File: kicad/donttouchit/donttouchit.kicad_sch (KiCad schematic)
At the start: 52 parts, among them J1 Conn_01x02_Female, J10 Conn_01x04_Male, J2 Conn_01x02_Female, J3 Conn_01x02_Female, J4 Conn_01x02_Female, J5 Conn_01x02_Female, J6 Conn_01x02_Female, J7 Conn_01x02_Female, J8 Conn_01x02_Female, J9 Conn_01x02_Female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

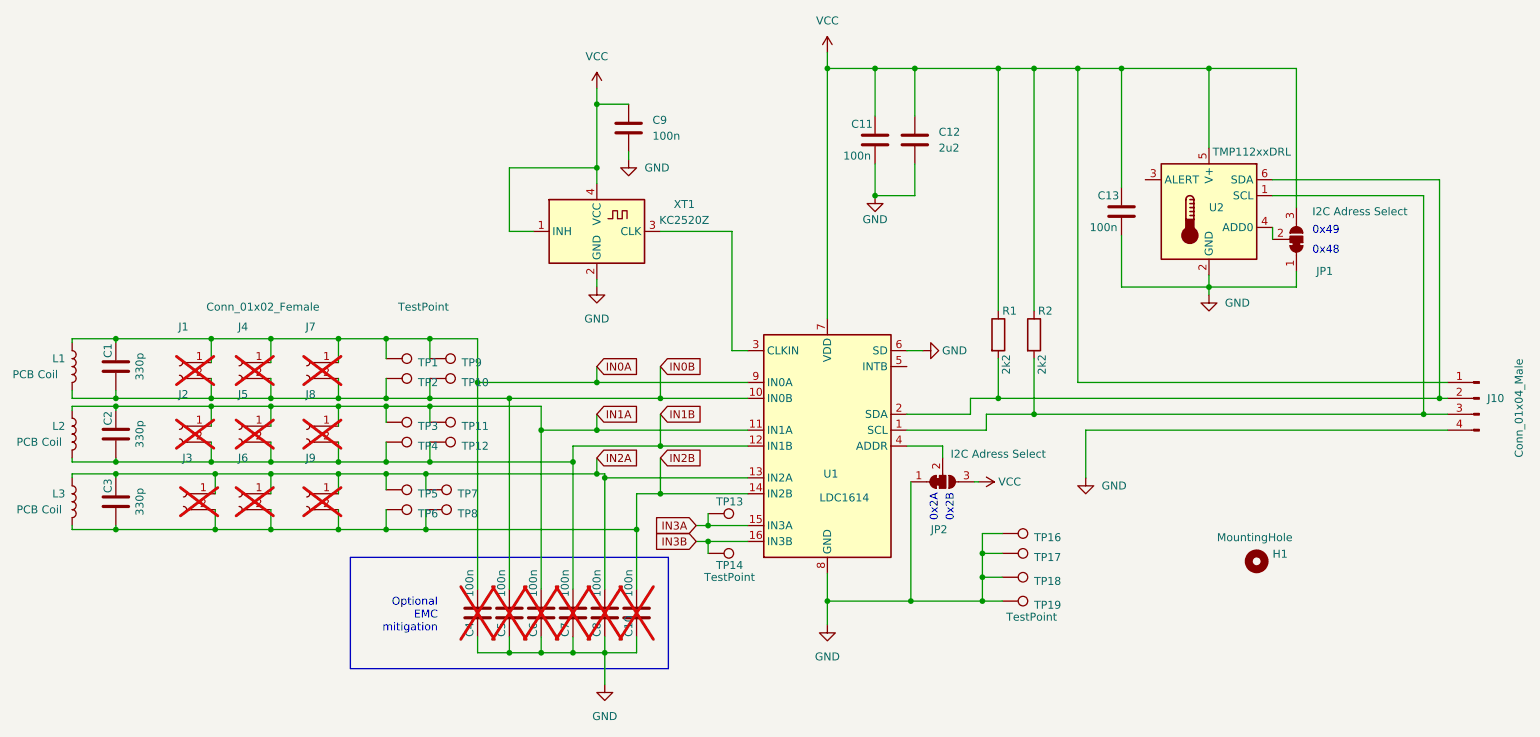
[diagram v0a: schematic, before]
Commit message: smaller formfactor that fits in the space of an Omron probe, 4th sensor pads removed
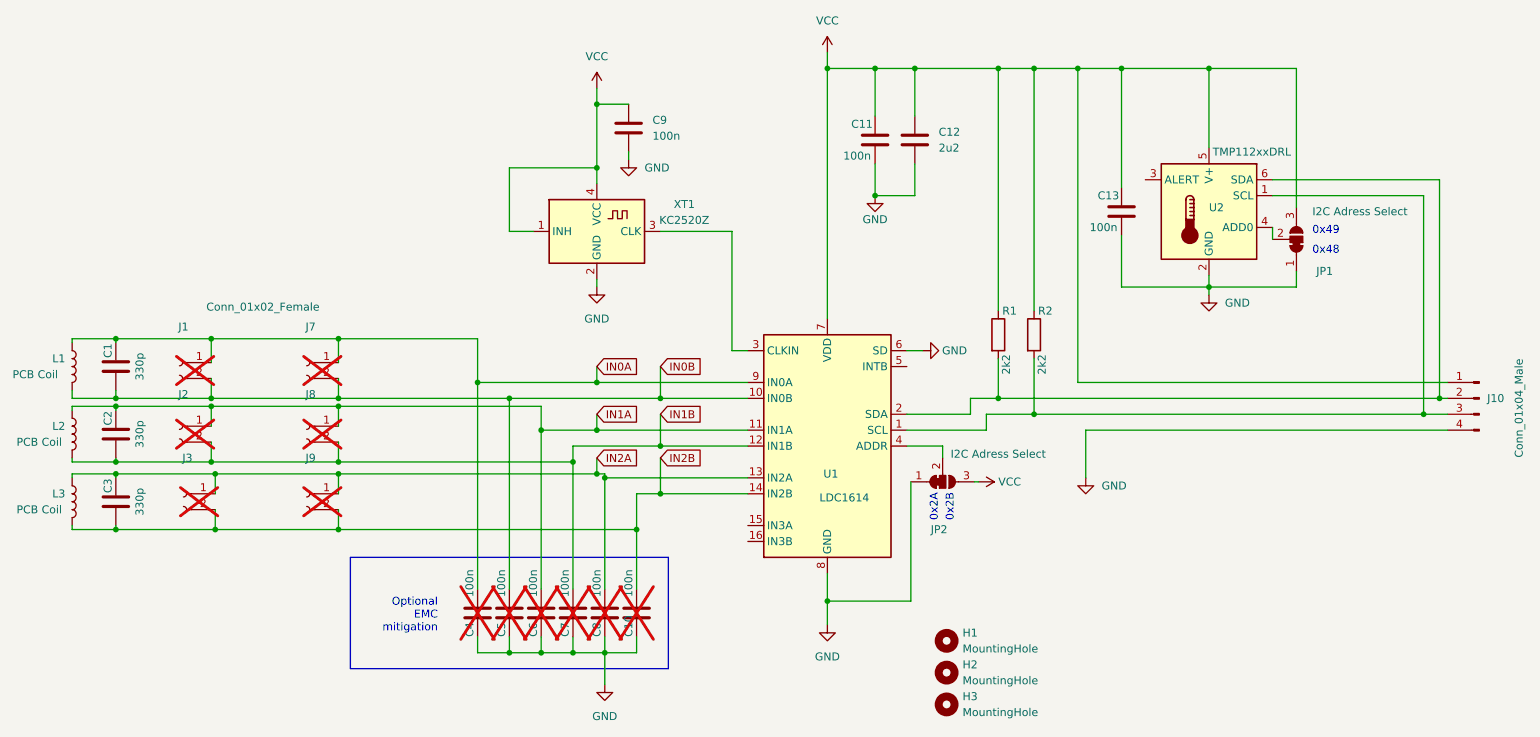
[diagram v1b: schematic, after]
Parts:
- removed J4, J5, J6: Conn_01x02_Female, Library:PCBConnPads, symbol Connector:Conn_01x02_Female
- removed TP1, TP10, TP11, TP12, TP13, TP14, TP16, TP17, TP18, TP19, TP2, TP3, TP4, TP5, TP6, TP7, TP8, TP9: TestPoint, TestPoint:TestPoint_THTPad_1.5x1.5mm_Drill0.7mm, symbol Connector:TestPoint
- added H2, H3: MountingHole, MountingHole:MountingHole_3.5mm, symbol Mechanical:MountingHole
- H1: footprint MountingHole:MountingHole_3.2mm_M3 -> MountingHole:MountingHole_3.5mm
- J1, J2, J3: footprint Library:PCBConnPads -> Library:PCBConnPadsTHT
- J7, J8, J9: footprint Library:PCBConnPadsLong -> Library:PCBConnPadsTHT
- L1, L2, L3: footprint Library:Coil -> Library:Coil_14x14
- U1: footprint Package_DFN_QFN:WQFN-16-1EP_4x4mm_P0.5mm_EP2.6x2.6mm_ThermalVias -> Library:WQFN-16-1EP_4x4mm_P0.5mm_EP2.6x2.6mm_ThermalVias
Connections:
- net IN3A: no longer names the net of U1.15 (IN3A)
- net IN3B: no longer names the net of U1.16 (IN3B)

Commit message: ESD capacitor values corrected / Tempsensor name updated
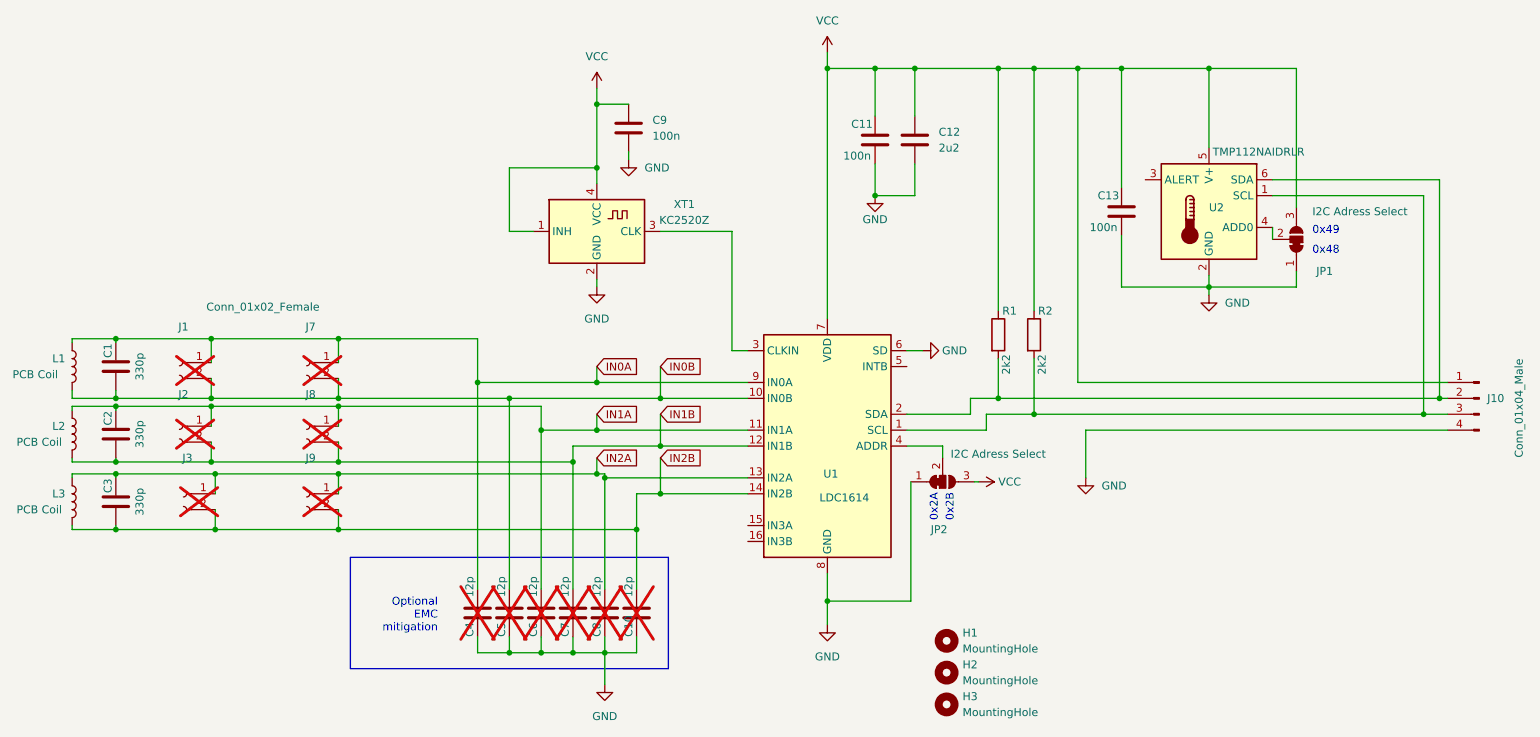
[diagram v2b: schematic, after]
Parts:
- C10, C4, C5, C6, C7, C8: value 100n -> 12p
- U2: value TMP112xxDRL -> TMP112NAIDRLR
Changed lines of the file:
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@@
       (effects (font (size 1.27 1.27)) (justify left))
     )
-    (property "Value" "100n" (at 134.62 135.255 90)
+    (property "Value" "12p" (at 134.62 135.255 90)
       (effects (font (size 1.27 1.27)) (justify left))
     )
@@
       (effects (font (size 1.27 1.27)) (justify left))
     )
-    (property "Value" "100n" (at 124.46 135.255 90)
+    (property "Value" "12p" (at 124.46 135.255 90)
       (effects (font (size 1.27 1.27)) (justify left))
     )
@@
       (effects (font (size 1.27 1.27)) (justify left))
     )
-    (property "Value" "100n" (at 114.3 135.255 90)
+    (property "Value" "12p" (at 114.3 135.255 90)
       (effects (font (size 1.27 1.27)) (justify left))
     )
@@
       (effects (font (size 1.27 1.27)) (justify left))
     )
-    (property "Value" "100n" (at 129.54 135.255 90)
+    (property "Value" "12p" (at 129.54 135.255 90)
       (effects (font (size 1.27 1.27)) (justify left))
     )
@@
       (effects (font (size 1.27 1.27)) (justify left))
     )
-    (property "Value" "100n" (at 119.38 135.255 90)
+    (property "Value" "12p" (at 119.38 135.255 90)
       (effects (font (size 1.27 1.27)) (justify left))
     )
@@
       (effects (font (size 1.27 1.27)) (justify left))
     )
-    (property "Value" "100n" (at 139.7 135.255 90)
+    (property "Value" "12p" (at 139.7 135.255 90)
       (effects (font (size 1.27 1.27)) (justify left))
     )
@@
       (effects (font (size 1.27 1.27)) (justify right))
     )
-    (property "Value" "TMP112xxDRL" (at 232.9941 64.135 0)
+    (property "Value" "TMP112NAIDRLR" (at 232.9941 64.135 0)
       (effects (font (size 1.27 1.27)) (justify right))
     )
